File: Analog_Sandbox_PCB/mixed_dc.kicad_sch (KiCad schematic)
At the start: 13 parts, among them J10 PAD, J11 PAD, J8 PAD, J9 PAD, U1 Current Source

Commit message: slight update
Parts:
- U1: footprint Analog_Sandbox_PCB:TO92260P521H934-3 -> Connector_PinSocket_2.54mm:PinSocket_1x03_P2.54mm_Vertical
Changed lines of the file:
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@@
 			)
 		)
-		(property "Footprint" "Analog_Sandbox_PCB:TO92260P521H934-3"
+		(property "Footprint" "Connector_PinSocket_2.54mm:PinSocket_1x03_P2.54mm_Vertical"
 			(at 93.98 71.12 0)
 			(effects

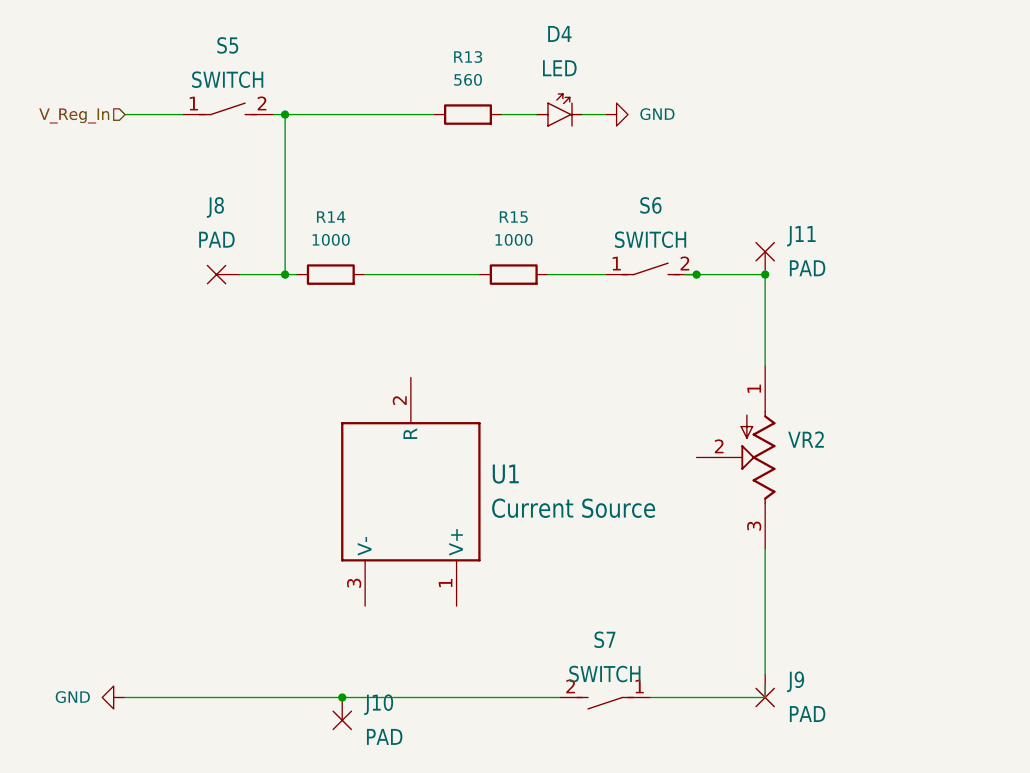
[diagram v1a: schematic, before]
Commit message: Config LM134
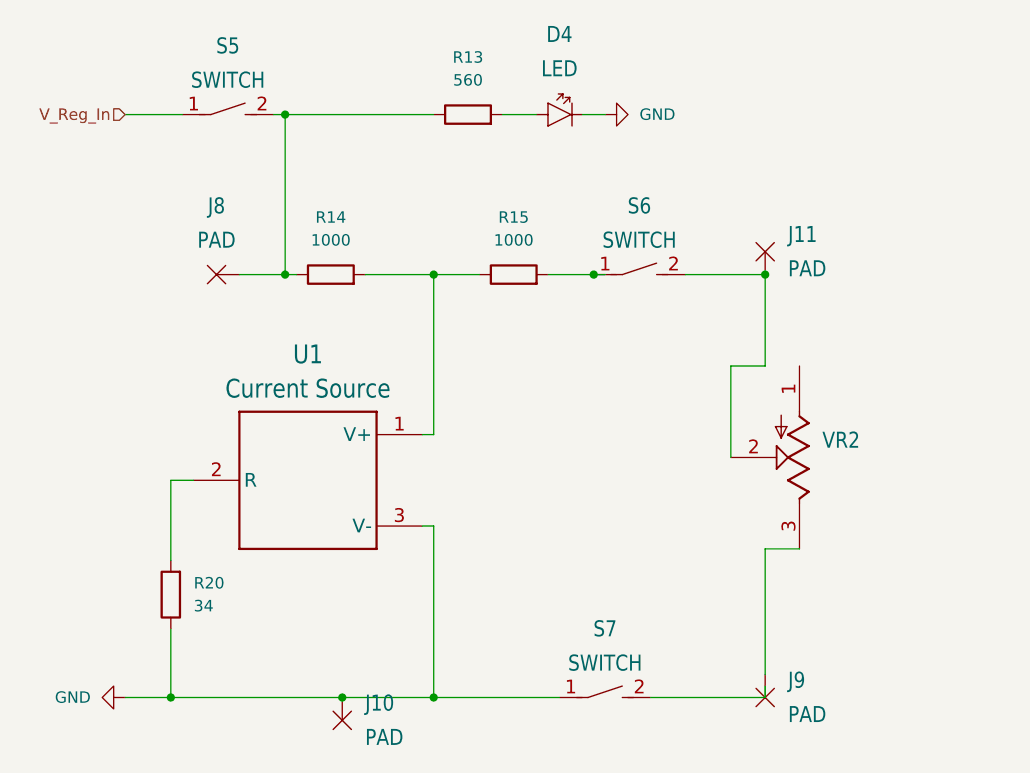
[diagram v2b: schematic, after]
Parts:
- added R20: 34, Resistor_SMD:R_2010_5025Metric_Pad1.40x2.65mm_HandSolder, symbol Device:R
- S5, S6, S7: footprint Analog_Sandbox_PCB:DS-01 -> Button_Switch_THT:SW_DIP_SPSTx01_Slide_9.78x4.72mm_W7.62mm_P2.54mm
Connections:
- net GND: now also S7.1, U1.3 (V-), R20.1; no longer S7.2
- net at J11.1 (P), S6.2: now also VR2.2 (WIPER); no longer VR2.1 (CCW)
- net at R14.2, R15.1: now also U1.1 (V+)
- net at U1.2 (R): now also R20.2
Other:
- moved on the sheet: U1, VR2

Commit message: All Circuits Added, Layout Almost done
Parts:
- removed D4: LED, Diode_SMD:D_2010_5025Metric_Pad1.52x2.65mm_HandSolder, symbol Analog_Sandbox_PCB-eagle-import:CHIP-FLAT-Y_0603-0.35MM
- added D4: LED, Diode_SMD:D_1206_3216Metric, symbol Device:LED
- J10: footprint Analog_Sandbox_PCB:2.54_1.0 -> 2.54_1.0_16378166
- R20: value 34 -> 33
- VR2: footprint Analog_Sandbox_PCB:TRIM_3362P-1-102LF -> TRIM_3362P-1-102LF_vf.A5S3VpQGRRqLSuxbPYtLvA
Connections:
- net GND: now also D4.1 (K)
- net at S7.2: now also J9.1 (P), VR2.3 (CW)
- net at R13.2: now also D4.2 (A)
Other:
- moved on the sheet: J9, S6
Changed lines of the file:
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@@
 	(paper "A5")
+	(junction
+		(at 114.3 29.21)
+		(diameter 0)
+		(color 0 0 0 0)
+	)
 	(junction
 		(at 80.01 46.99)
@@
 	)
 	(junction
-		(at 114.3 46.99)
+		(at 106.68 29.21)
 		(diameter 0)
 		(color 0 0 0 0)
@@
 		(color 0 0 0 0)
 	)
+	(junction
+		(at 133.35 92.71)
+		(diameter 0)
+		(color 0 0 0 0)
+	)
 	(wire
 		(pts
@@
 	(wire
 		(pts
-			(xy 114.3 46.99) (xy 115.57 46.99)
-		)
-		(stroke
-			(width 0)
-			(type default)
-		)
-	)
-	(wire
-		(pts
 			(xy 96.52 93.98) (xy 110.49 93.98)
 		)
@@
 	(wire
 		(pts
-			(xy 104.14 29.21) (xy 107.95 29.21)
+			(xy 104.14 29.21) (xy 106.68 29.21)
 		)
 		(stroke
@@
 	(wire
 		(pts
-			(xy 124.46 46.99) (xy 133.35 46.99)
+			(xy 121.92 46.99) (xy 133.35 46.99)
 		)
 		(stroke
@@
 	(wire
 		(pts
-			(xy 115.57 29.21) (xy 113.03 29.21)
+			(xy 115.57 29.21) (xy 114.3 29.21)
 		)
 		(stroke
@@
 	(wire
 		(pts
-			(xy 109.22 46.99) (xy 114.3 46.99)
+			(xy 114.3 29.21) (xy 113.03 29.21)
+		)
+		(stroke
+			(width 0)
+			(type default)
+		)
+	)
+	(wire
+		(pts
+			(xy 106.68 29.21) (xy 107.95 29.21)
 		)
 		(stroke
@@
 	(wire
 		(pts
-			(xy 133.35 77.47) (xy 133.35 91.44)
+			(xy 133.35 77.47) (xy 133.35 92.71)
 		)
 		(stroke
@@
 		(pts
 			(xy 80.01 29.21) (xy 96.52 29.21)
+		)
+		(stroke
+			(width 0)
+			(type default)
+		)
+	)
+	(wire
+		(pts
+			(xy 109.22 46.99) (xy 111.76 46.99)
 		)
 		(stroke
@@
 	(symbol
 		(lib_id "Analog_Sandbox_PCB-eagle-import:DS01E")
-		(at 119.38 46.99 0)
+		(at 116.84 46.99 0)
 		(unit 1)
 		(exclude_from_sim no)
@@
 		(fields_autoplaced yes)
 		(property "Reference" "S6"
-			(at 119.38 39.37 0)
+			(at 116.84 39.37 0)
 			(effects
 				(font
@@
 		)
 		(property "Value" "SWITCH"
-			(at 119.38 43.18 0)
+			(at 116.84 43.18 0)
 			(effects
 				(font
@@
 		)
 		(property "Footprint" "Button_Switch_THT:SW_DIP_SPSTx01_Slide_9.78x4.72mm_W7.62mm_P2.54mm"
-			(at 119.38 46.99 0)
+			(at 116.84 46.99 0)
 			(effects
 				(font
@@
 		)
 		(property "Datasheet" ""
-			(at 119.38 46.99 0)
+			(at 116.84 46.99 0)
 			(effects
 				(font
@@
 		)
 		(property "Description" "DIL/CODE Switch"
-			(at 119.38 46.99 0)
+			(at 116.84 46.99 0)
 			(effects
 				(font
@@
 			)
 		)
-		(property "Value" "34"
+		(property "Value" "33"
 			(at 69.85 83.8199 0)
 			(effects
@@
 	)
 	(symbol
-		(lib_id "Analog_Sandbox_PCB-eagle-import:CHIP-FLAT-Y_0603-0.35MM")
-		(at 110.49 29.21 0)
-		(unit 1)
-		(exclude_from_sim no)
-		(in_bom yes)
-		(on_board yes)
-		(dnp no)
-		(fields_autoplaced yes)
-		(property "Reference" "D4"
-			(at 110.49 20.32 0)
-			(effects
-				(font
-					(size 1.778 1.5113)
-				)
-			)
-		)
-		(property "Value" "LED"
-			(at 110.49 24.13 0)
-			(effects
-				(font
-					(size 1.778 1.5113)
-				)
-			)
-		)
-		(property "Footprint" "Diode_SMD:D_2010_5025Metric_Pad1.52x2.65mm_HandSolder"
-			(at 110.49 29.21 0)
-			(effects
-				(font
-					(size 1.27 1.27)
-				)
-				(hide yes)
-			)
-		)
-		(property "Datasheet" ""
-			(at 110.49 29.21 0)
-			(effects
-				(font
-					(size 1.27 1.27)
-				)
-				(hide yes)
-			)
-		)
-		(property "Description" "Yellow LED - Generic"
-			(at 110.49 29.21 0)
-			(effects
-				(font
-					(size 1.27 1.27)
-				)
-				(hide yes)
-			)
-		)
-		(pin "A"
-		)
-		(pin "C"
-		)
-		(instances
-			(project "Analog_Sandbox_PCB"
-				(path "/ac750111-a1db-4b3c-a106-e1424e47aebb/1ffce373-b0c0-4221-ae7b-13552ac0c0a1"
-					(reference "D4")
-					(unit 1)
-				)
-			)
-		)
-	)
-	(symbol
 		(lib_id "Analog_Sandbox_PCB-eagle-import:3362P-1-102LF")
 		(at 137.16 67.31 270)
@@
 			)
 		)
-		(property "Footprint" "Analog_Sandbox_PCB:TRIM_3362P-1-102LF"
+		(property "Footprint" "TRIM_3362P-1-102LF_vf.A5S3VpQGRRqLSuxbPYtLvA"
 			(at 137.16 67.31 0)
 			(effects
@@
 			)
 		)
-		(property "Footprint" "Analog_Sandbox_PCB:2.54_1.0"
+		(property "Footprint" "2.54_1.0_16378166"
 			(at 86.36 96.52 0)
 			(effects
@@
 	)
 	(symbol
+		(lib_id "Device:LED")
+		(at 110.49 29.21 180)
+		(unit 1)
+		(exclude_from_sim no)
+		(in_bom yes)
+		(on_board yes)
+		(dnp no)
+		(fields_autoplaced yes)
+		(property "Reference" "D4"
+			(at 112.0775 21.59 0)
+			(effects
+				(font
+					(size 1.27 1.27)
+				)
+			)
+		)
+		(property "Value" "LED"
+			(at 112.0775 24.13 0)
+			(effects
+				(font
+					(size 1.27 1.27)
+				)
+			)
+		)
+		(property "Footprint" "Diode_SMD:D_1206_3216Metric"
+			(at 110.49 29.21 0)
+			(effects
+				(font
+					(size 1.27 1.27)
+				)
+				(hide yes)
+			)
+		)
+		(property "Datasheet" "~"
+			(at 110.49 29.21 0)
+			(effects
+				(font
+					(size 1.27 1.27)
+				)
+				(hide yes)
+			)
+		)
+		(property "Description" "Light emitting diode"
+			(at 110.49 29.21 0)
+			(effects
+				(font
+					(size 1.27 1.27)
+				)
+				(hide yes)
+			)
+		)
+		(property "Sim.Pins" "1=K 2=A"
+			(at 110.49 29.21 0)
+			(effects
+				(font
+					(size 1.27 1.27)
+				)
+				(hide yes)
+			)
+		)
+		(pin "1"
+		)
+		(pin "2"
+		)
+		(instances
+			(project "Analog_Sandbox_PCB"
+				(path "/ac750111-a1db-4b3c-a106-e1424e47aebb/1ffce373-b0c0-4221-ae7b-13552ac0c0a1"
+					(reference "D4")
+					(unit 1)
+				)
+			)
+		)
+	)
+	(symbol
 		(lib_id "power:GND")
 		(at 62.23 93.98 270)
@@
 	(symbol
 		(lib_id "Analog_Sandbox_PCB-eagle-import:PAD")
-		(at 133.35 93.98 90)
+		(at 133.35 95.25 90)
 		(unit 1)
 		(exclude_from_sim no)
@@
 		(fields_autoplaced yes)
 		(property "Reference" "J9"
-			(at 135.89 92.075 90)
+			(at 135.89 93.345 90)
 			(effects
 				(font
@@
 		)
 		(property "Value" "PAD"
-			(at 135.89 95.885 90)
+			(at 135.89 97.155 90)
 			(effects
 				(font
@@
 		)
 		(property "Footprint" "Analog_Sandbox_PCB:2.54_1.0"
-			(at 133.35 93.98 0)
+			(at 133.35 95.25 0)
 			(effects
 				(font
@@
 		)
 		(property "Datasheet" ""
-			(at 133.35 93.98 0)
+			(at 133.35 95.25 0)
 			(effects
 				(font
@@
 		)
 		(property "Description" "Through-Hole Pad"
-			(at 133.35 93.98 0)
-			(effects
-				(font
+			(at 133.35 95.25 0)
+			(effects
+				(font

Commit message: fin
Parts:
- removed J10: PAD, 2.54_1.0_16378166, symbol Analog_Sandbox_PCB-eagle-import:PAD
- removed VR2: ~, TRIM_3362P-1-102LF_vf.A5S3VpQGRRqLSuxbPYtLvA, symbol Analog_Sandbox_PCB-eagle-import:3362P-1-102LF
- added R31: 3362P-1-103LF, Sandbox:POT_3362P, symbol 3362p:3362P-1-103LF
- J11, J8, J9: footprint Analog_Sandbox_PCB:2.54_1.0 -> TestPoint:TestPoint_Loop_D2.50mm_Drill1.85mm
- R13, R14, R15, R20: footprint Resistor_SMD:R_2010_5025Metric_Pad1.40x2.65mm_HandSolder -> Resistor_SMD:R_1206_3216Metric
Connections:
- net GND: now also R31.3
- net at J11.1 (P), S6.2: now also R31.2
- net at J9.1 (P), S7.2: now also R31.1

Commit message: made changes from morning of 4/13
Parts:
- renumbered J8 to M1, J11 to M2, J9 to M3
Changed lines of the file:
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@@
 		(dnp no)
 		(fields_autoplaced yes)
-		(property "Reference" "J11"
+		(property "Reference" "M2"
 			(at 135.89 42.545 90)
 			(effects
@@
 			(project "Analog_Sandbox_PCB"
 				(path "/ac750111-a1db-4b3c-a106-e1424e47aebb/1ffce373-b0c0-4221-ae7b-13552ac0c0a1"
-					(reference "J11")
+					(reference "M2")
 					(unit 1)
 				)
@@
 		(dnp no)
 		(fields_autoplaced yes)
-		(property "Reference" "J9"
+		(property "Reference" "M3"
 			(at 135.89 94.615 90)
 			(effects
@@
 			(project "Analog_Sandbox_PCB"
 				(path "/ac750111-a1db-4b3c-a106-e1424e47aebb/1ffce373-b0c0-4221-ae7b-13552ac0c0a1"
-					(reference "J9")
+					(reference "M3")
 					(unit 1)
 				)
@@
 		(dnp no)
 		(fields_autoplaced yes)
-		(property "Reference" "J8"
+		(property "Reference" "M1"
 			(at 72.39 39.37 0)
 			(effects
@@
 			(project "Analog_Sandbox_PCB"
 				(path "/ac750111-a1db-4b3c-a106-e1424e47aebb/1ffce373-b0c0-4221-ae7b-13552ac0c0a1"
-					(reference "J8")
-					(unit 1)
-				)
+					(reference "M1")
+					(unit 1)
+				)

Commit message: final changes addded
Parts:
- added M4, M5: PAD, TestPoint:TestPoint_Loop_D2.50mm_Drill1.85mm, symbol Analog_Sandbox_PCB-eagle-import:PAD
- added R22: 1000, Resistor_SMD:R_1206_3216Metric, symbol Device:R
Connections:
- net at R14.2, R15.1: now also M4.1 (P), R22.2; no longer U1.1 (V+)
- new net: M5.1 (P), R22.1, U1.1 (V+)
